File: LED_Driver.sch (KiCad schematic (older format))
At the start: 0 parts

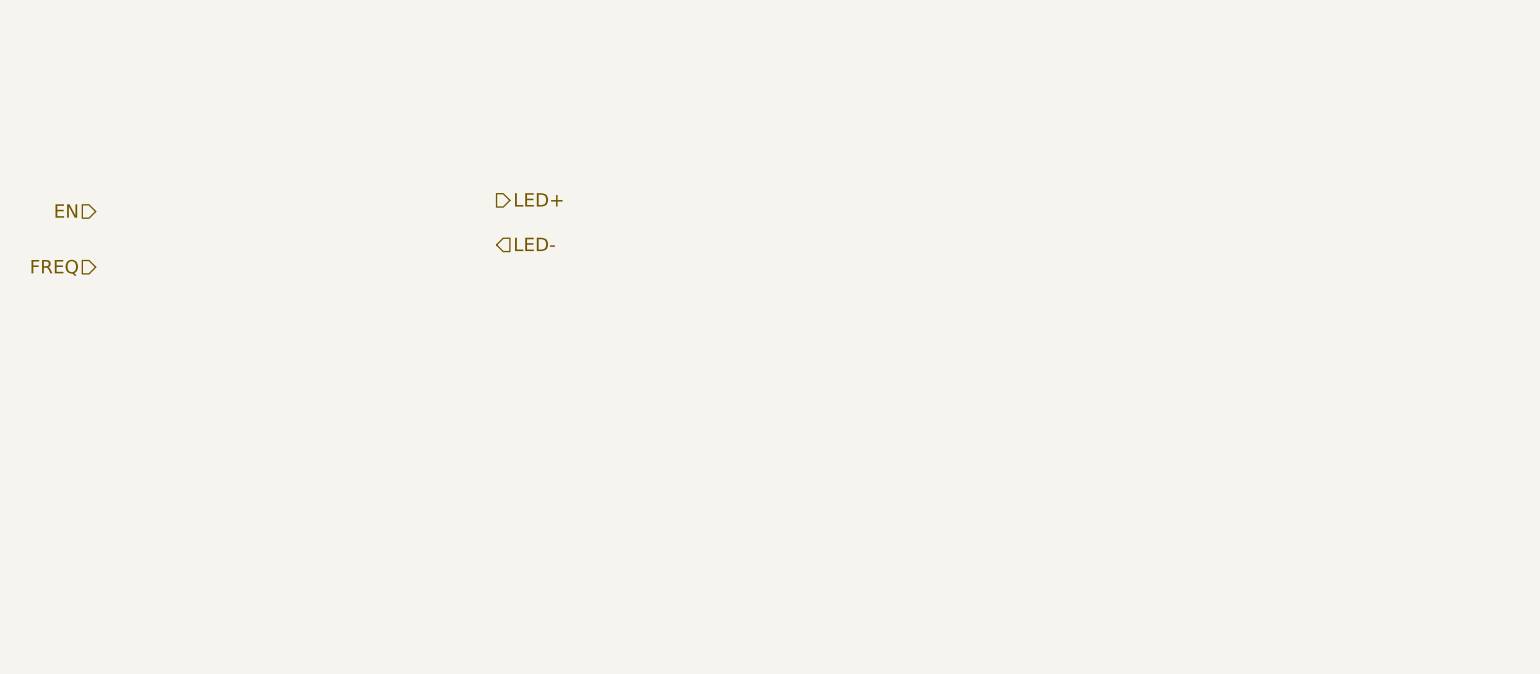
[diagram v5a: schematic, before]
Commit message: Created first schematic for LED module
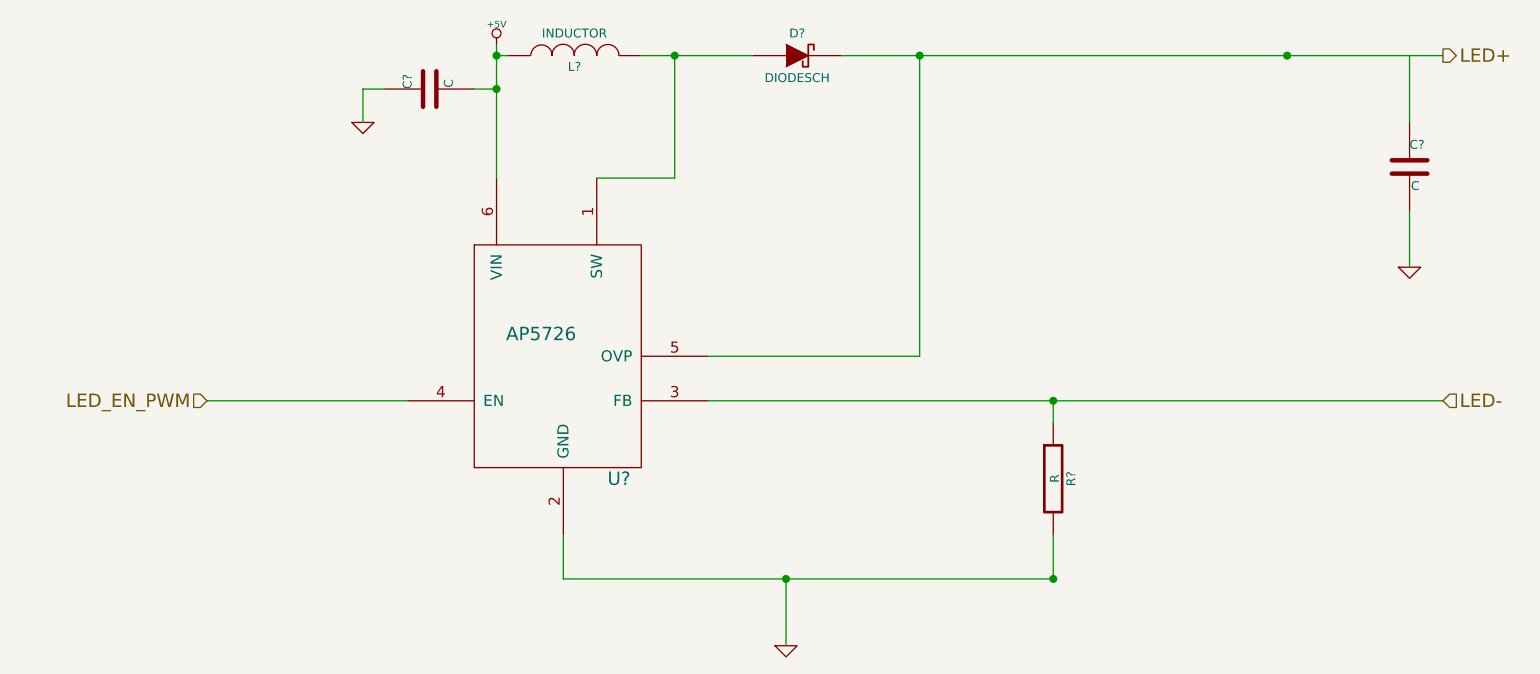
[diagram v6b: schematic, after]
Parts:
- added C? (x2): C, ~, symbol C
- added D?: DIODESCH, ~, symbol DIODESCH
- added L?: INDUCTOR, ~, symbol INDUCTOR
- added R?: R, ~, symbol R
- added U?: AP5726, symbol AP5726
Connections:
- net labels added: +5V, GND, LED_EN_PWM
- net labels removed: EN, FREQ
- wire segments 0 -> 27
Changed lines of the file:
@@
 $Descr A4 11693 8268
 encoding utf-8
-Sheet 6 9
+Sheet 5 9
 Title ""
 Date "10 feb 2014"
@@
 Comment4 ""
 $EndDescr
-Text HLabel 2600 2050 0    60   Input ~ 0
-EN
-Text HLabel 2600 2300 0    60   Input ~ 0
-FREQ
-Text HLabel 4400 2000 2    60   Output ~ 0
+Text HLabel 3100 2900 0    60   Input ~ 0
+LED_EN_PWM
+Text HLabel 8650 1350 2    60   Output ~ 0
 LED+
-Text HLabel 4400 2200 2    60   Input ~ 0
+Text HLabel 8650 2900 2    60   Input ~ 0
 LED-
+$Comp
+L AP5726 U?
+U 1 1 52F8483D
+P 4600 2800
+F 0 "U?" H 4950 2350 60  0000 C CNN
+F 1 "AP5726" H 4600 3000 60  0000 C CNN
+F 2 "" H 4600 2800 60  0000 C CNN
+F 3 "" H 4600 2800 60  0000 C CNN
+	1    4600 2800
+	1    0    0    -1
+$EndComp
+Wire Wire Line
+	3100 2900 4000 2900
+$Comp
+L +5V #PWR?
+U 1 1 52F84ACD
+P 4400 1300
+F 0 "#PWR?" H 4400 1390 20  0001 C CNN
+F 1 "+5V" H 4400 1390 30  0000 C CNN
+F 2 "" H 4400 1300 60  0000 C CNN
+F 3 "" H 4400 1300 60  0000 C CNN
+	1    4400 1300
+	1    0    0    -1
+$EndComp
+$Comp
+L GND #PWR?
+U 1 1 52F84ADC
+P 3800 1650
+F 0 "#PWR?" H 3800 1650 30  0001 C CNN
+F 1 "GND" H 3800 1580 30  0001 C CNN
+F 2 "" H 3800 1650 60  0000 C CNN
+F 3 "" H 3800 1650 60  0000 C CNN
+	1    3800 1650
+	1    0    0    -1
+$EndComp
+Wire Wire Line
+	4400 1300 4400 1350
+Wire Wire Line
+	4400 1350 4400 1500
+Wire Wire Line
+	4400 1500 4400 1900
+$Comp
+L C C?
+U 1 1 52F84B01
+P 4100 1500
+F 0 "C?" H 4100 1600 40  0000 L CNN
+F 1 "C" H 4106 1415 40  0000 L CNN
+F 2 "~" H 4138 1350 30  0000 C CNN
+F 3 "~" H 4100 1500 60  0000 C CNN
+	1    4100 1500
+	0    -1   -1   0
+$EndComp
+Wire Wire Line
+	3900 1500 3800 1500
+Wire Wire Line
+	3800 1500 3800 1650
+$Comp
+L INDUCTOR L?
+U 1 1 52F84B22
+P 4750 1350
+F 0 "L?" V 4700 1350 40  0000 C CNN
+F 1 "INDUCTOR" V 4850 1350 40  0000 C CNN
+F 2 "~" H 4750 1350 60  0000 C CNN
+F 3 "~" H 4750 1350 60  0000 C CNN
+	1    4750 1350
+	0    -1   -1   0
+$EndComp
+Wire Wire Line
+	4300 1500 4400 1500
+Connection ~ 4400 1500
+Wire Wire Line
+	4450 1350 4400 1350
+Connection ~ 4400 1350
+Wire Wire Line
+	5050 1350 5200 1350
+Wire Wire Line
+	5200 1350 5550 1350
+Wire Wire Line
+	5200 1350 5200 1900
+Wire Wire Line
+	5200 1900 4850 1900
+$Comp
+L DIODESCH D?
+U 1 1 52F84B4A
+P 5750 1350
+F 0 "D?" H 5750 1450 40  0000 C CNN
+F 1 "DIODESCH" H 5750 1250 40  0000 C CNN
+F 2 "~" H 5750 1350 60  0000 C CNN
+F 3 "~" H 5750 1350 60  0000 C CNN
+	1    5750 1350
+	1    0    0    -1
+$EndComp
+Connection ~ 5200 1350
+Wire Wire Line
+	5350 2700 6300 2700
+Wire Wire Line
+	6300 2700 6300 1350
+Wire Wire Line
+	5950 1350 6300 1350
+Wire Wire Line
+	6300 1350 7950 1350
+Wire Wire Line
+	7950 1350 8650 1350
+$Comp
+L R R?
+U 1 1 52F84B73
+P 6900 3250
+F 0 "R?" V 6980 3250 40  0000 C CNN
+F 1 "R" V 6907 3251 40  0000 C CNN
+F 2 "~" V 6830 3250 30  0000 C CNN
+F 3 "~" H 6900 3250 30  0000 C CNN
+	1    6900 3250
+	1    0    0    -1
+$EndComp
+Wire Wire Line
+	5350 2900 6900 2900
+Wire Wire Line
+	6900 2900 8650 2900
+Wire Wire Line
+	6900 2900 6900 3000
+Wire Wire Line
+	4700 3500 4700 3700
+Wire Wire Line
+	6900 3700 6900 3500
+$Comp
+L C C?
+U 1 1 52F84BA7
+P 8500 1850
+F 0 "C?" H 8500 1950 40  0000 L CNN
+F 1 "C" H 8506 1765 40  0000 L CNN
+F 2 "~" H 8538 1700 30  0000 C CNN
+F 3 "~" H 8500 1850 60  0000 C CNN
+	1    8500 1850
+	1    0    0    -1
+$EndComp
+Connection ~ 6900 3700
+Wire Wire Line
+	8500 1350 8500 1650
+Connection ~ 6300 1350
+$Comp
+L GND #PWR?
+U 1 1 52F84BE2
+P 5700 4000
+F 0 "#PWR?" H 5700 4000 30  0001 C CNN
+F 1 "GND" H 5700 3930 30  0001 C CNN
+F 2 "" H 5700 4000 60  0000 C CNN
+F 3 "" H 5700 4000 60  0000 C CNN
+	1    5700 4000
+	1    0    0    -1
+$EndComp
+Wire Wire Line
+	5700 4000 5700 3700
+Connection ~ 5700 3700
+Connection ~ 7950 1350
+$Comp
+L GND #PWR?
+U 1 1 52F84C43
+P 8500 2300
+F 0 "#PWR?" H 8500 2300 30  0001 C CNN
+F 1 "GND" H 8500 2230 30  0001 C CNN
+F 2 "" H 8500 2300 60  0000 C CNN
+F 3 "" H 8500 2300 60  0000 C CNN
+	1    8500 2300
+	1    0    0    -1
+$EndComp
+Wire Wire Line
+	8500 2300 8500 2050
+Wire Wire Line
+	4700 3700 5700 3700
+Wire Wire Line
+	5700 3700 6900 3700
+Connection ~ 6900 2900
 $EndSCHEMATC

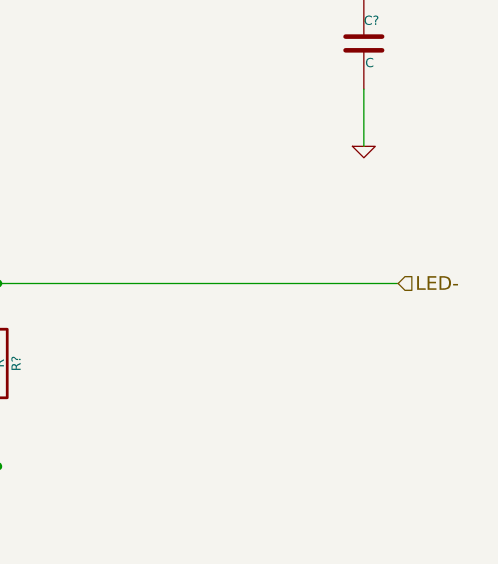
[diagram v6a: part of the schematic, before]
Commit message: Created the Arduino module and then connected all the modules in the main schematic
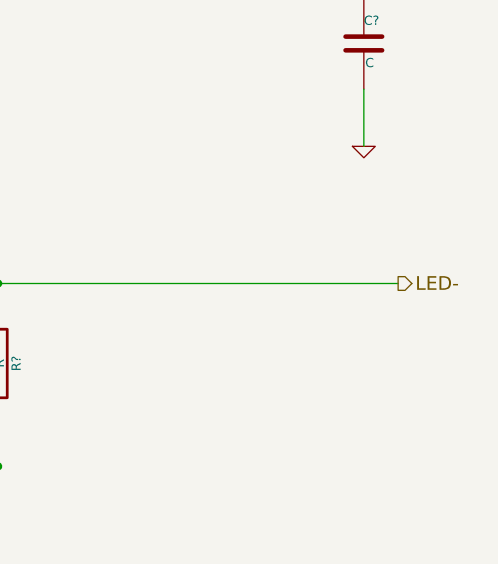
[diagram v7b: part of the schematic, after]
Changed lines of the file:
@@
 Text HLabel 8650 1350 2    60   Output ~ 0
 LED+
-Text HLabel 8650 2900 2    60   Input ~ 0
+Text HLabel 8650 2900 2    60   Output ~ 0
 LED-
 $Comp
